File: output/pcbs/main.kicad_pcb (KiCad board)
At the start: 2 copper layers, 103.3 x 88.5 mm, 113 parts, among them SW1 CPG1316S01D02_reversible, SW10 CPG1316S01D02_reversible, SW11 CPG1316S01D02_reversible, SW12 CPG1316S01D02_reversible, SW13 CPG1316S01D02_reversible, SW14 CPG1316S01D02_reversible, SW15 CPG1316S01D02_reversible, SW16 CPG1316S01D02_reversible, SW17 CPG1316S01D02_reversible, SW18 CPG1316S01D02_reversible, SW2 CPG1316S01D02_reversible, SW3 CPG1316S01D02_reversible, SW4 CPG1316S01D02_reversible, SW5 CPG1316S01D02_reversible, SW6 CPG1316S01D02_reversible, SW7 CPG1316S01D02_reversible, SW8 CPG1316S01D02_reversible, SW9 CPG1316S01D02_reversible

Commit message: fix(routing): route pcb
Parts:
- removed the REF** at (2.80, 5.10)
- removed the REF** at (53.8, -6.80)
- removed the REF** at (53.8, -23.8)
- removed the REF** at (53.8, -40.8)
- removed the REF** at (70.8, -3.40)
- removed the REF** at (70.8, -20.4)
- removed the REF** at (70.8, -37.4)
- removed the REF** at (47.0, 13.6)
- removed the REF** at (64.5, 15.5)
- removed the REF** at (82.5, 19.9)
- removed the REF** at (-2.80, 5.10)
- removed the REF** at (2.80, -11.9)
- removed the REF** at (-2.80, -11.9)
- removed the REF** at (-2.80, -28.9)
- removed the REF** at (14.2, -8.50)
- removed the REF** at (14.2, -25.5)
- removed the REF** at (14.2, -42.5)
- removed the REF** at (31.2, -15.3)
- removed the REF** at (31.2, -32.3)
- removed the REF** at (31.2, -49.3)
- removed the REF** at (48.2, -6.80)
- removed the REF** at (48.2, -23.8)
- removed the REF** at (2.80, -28.9)
- removed the REF** at (48.2, -40.8)
- removed the REF** at (65.2, -3.40)
- removed the REF** at (65.2, -20.4)
- removed the REF** at (65.2, -37.4)
- removed the REF** at (41.4, 13.6)
- removed the REF** at (59.0, 14.5)
- removed the REF** at (77.7, 17.1)
- removed the REF** at (0.00, -3.67)
- removed the REF** at (0.00, -20.7)
- removed the REF** at (0.00, -37.7)
- removed the REF** at (19.8, -8.50)
- removed the REF** at (17.0, -17.3)
- removed the REF** at (17.0, -34.3)
- removed the REF** at (17.0, -51.3)
- removed the REF** at (34.0, -24.1)
- removed the REF** at (34.0, -41.1)
- removed the REF** at (34.0, -58.1)
- removed the REF** at (51.0, -15.6)
- removed the REF** at (51.0, -32.6)
- removed the REF** at (51.0, -49.6)
- removed the REF** at (68.0, -12.2)
- removed the REF** at (19.8, -25.5)
- removed the REF** at (68.0, -29.2)
- removed the REF** at (68.0, -46.2)
- removed the REF** at (44.2, 4.83)
- removed the REF** at (63.3, 6.37)
- removed the REF** at (84.5, 10.9)
- removed the REF** at (0.00, -2.67)
- removed the REF** at (0.00, -19.7)
- removed the REF** at (0.00, -36.7)
- removed the REF** at (17.0, -16.3)
- removed the REF** at (17.0, -33.3)
- removed the REF** at (19.8, -42.5)
- removed the REF** at (17.0, -50.3)
- removed the REF** at (34.0, -23.1)
- removed the REF** at (34.0, -40.1)
- removed the REF** at (34.0, -57.1)
- removed the REF** at (51.0, -14.6)
- removed the REF** at (51.0, -31.6)
- removed the REF** at (51.0, -48.6)
- removed the REF** at (68.0, -11.2)
- removed the REF** at (68.0, -28.2)
- removed the REF** at (68.0, -45.2)
- removed the REF** at (36.8, -15.3)
- removed the REF** at (44.2, 5.83)
- removed the REF** at (63.1, 7.35)
- removed the REF** at (84.0, 11.8)
- removed the REF** at (36.8, -32.3)
- removed the REF** at (36.8, -49.3)
- added REF**: VIA-0.6mm, VIA-0.6mm, F.Cu at (254.4, 153.2)
- added REF**: VIA-0.6mm, VIA-0.6mm, F.Cu at (220.4, 134.5)
- added REF**: VIA-0.6mm, VIA-0.6mm, F.Cu at (220.4, 151.5)
- added REF**: VIA-0.6mm, VIA-0.6mm, F.Cu at (234.7, 153.4)
- added REF**: VIA-0.6mm, VIA-0.6mm, F.Cu at (203.4, 166.1)
- added REF**: VIA-0.6mm, VIA-0.6mm, F.Cu at (257.2, 144.9)
- added REF**: VIA-0.6mm, VIA-0.6mm, F.Cu at (254.4, 154.2)
- added REF**: VIA-0.6mm, VIA-0.6mm, F.Cu at (220.4, 135.5)
- added REF**: VIA-0.6mm, VIA-0.6mm, F.Cu at (217.7, 143.2)
- added REF**: VIA-0.6mm, VIA-0.6mm, F.Cu at (206.2, 173.8)
- added REF**: VIA-0.6mm, VIA-0.6mm, F.Cu at (237.4, 162.7)
- added REF**: VIA-0.6mm, VIA-0.6mm, F.Cu at (223.2, 177.2)
- added REF**: VIA-0.6mm, VIA-0.6mm, F.Cu at (223.2, 143.2)
- added REF**: VIA-0.6mm, VIA-0.6mm, F.Cu at (274.2, 182.3)
- added REF**: VIA-0.6mm, VIA-0.6mm, F.Cu at (271.4, 139.6)
- added REF**: VIA-0.6mm, VIA-0.6mm, F.Cu at (200.7, 173.8)
- added REF**: VIA-0.6mm, VIA-0.6mm, F.Cu at (268.6, 165.3)
- added REF**: VIA-0.6mm, VIA-0.6mm, F.Cu at (254.4, 137.2)
- added REF**: VIA-0.6mm, VIA-0.6mm, F.Cu at (268.6, 148.3)
- added REF**: VIA-0.6mm, VIA-0.6mm, F.Cu at (271.4, 173.6)
- added REF**: VIA-0.6mm, VIA-0.6mm, F.Cu at (240.2, 136.4)
- added REF**: VIA-0.6mm, VIA-0.6mm, F.Cu at (257.2, 178.9)
- added REF**: VIA-0.6mm, VIA-0.6mm, F.Cu at (237.4, 161.7)
- added REF**: VIA-0.6mm, VIA-0.6mm, F.Cu at (220.4, 168.5)
- added REF**: VIA-0.6mm, VIA-0.6mm, F.Cu at (271.4, 140.6)
- added REF**: VIA-0.6mm, VIA-0.6mm, F.Cu at (286.0, 205.7)
- added REF**: VIA-0.6mm, VIA-0.6mm, F.Cu at (274.2, 165.3)
- added REF**: VIA-0.6mm, VIA-0.6mm, F.Cu at (217.7, 160.2)
- added REF**: VIA-0.6mm, VIA-0.6mm, F.Cu at (251.7, 144.9)
- added REF**: VIA-0.6mm, VIA-0.6mm, F.Cu at (200.7, 190.8)
- added REF**: VIA-0.6mm, VIA-0.6mm, F.Cu at (254.4, 136.2)
- added REF**: VIA-0.6mm, VIA-0.6mm, F.Cu at (237.4, 127.7)
- added REF**: VIA-0.6mm, VIA-0.6mm, F.Cu at (251.7, 178.9)
- added REF**: VIA-0.6mm, VIA-0.6mm, F.Cu at (234.7, 136.4)
- added REF**: VIA-0.6mm, VIA-0.6mm, F.Cu at (250.4, 199.3)
- added REF**: VIA-0.6mm, VIA-0.6mm, F.Cu at (247.7, 190.6)
- added REF**: VIA-0.6mm, VIA-0.6mm, F.Cu at (240.2, 170.4)
- added REF**: VIA-0.6mm, VIA-0.6mm, F.Cu at (266.6, 193.1)
- added REF**: VIA-0.6mm, VIA-0.6mm, F.Cu at (281.1, 202.9)
- added REF**: VIA-0.6mm, VIA-0.6mm, F.Cu at (203.4, 149.1)
- added REF**: VIA-0.6mm, VIA-0.6mm, F.Cu at (244.8, 199.3)
- added REF**: VIA-0.6mm, VIA-0.6mm, F.Cu at (234.7, 170.4)
- added REF**: VIA-0.6mm, VIA-0.6mm, F.Cu at (203.4, 148.1)
- added REF**: VIA-0.6mm, VIA-0.6mm, F.Cu at (271.4, 156.6)
- added REF**: VIA-0.6mm, VIA-0.6mm, F.Cu at (254.4, 170.2)
- added REF**: VIA-0.6mm, VIA-0.6mm, F.Cu at (274.2, 148.3)
- added REF**: VIA-0.6mm, VIA-0.6mm, F.Cu at (237.4, 144.7)
- added REF**: VIA-0.6mm, VIA-0.6mm, F.Cu at (287.9, 196.7)
- added REF**: VIA-0.6mm, VIA-0.6mm, F.Cu at (271.4, 174.6)
- added REF**: VIA-0.6mm, VIA-0.6mm, F.Cu at (203.4, 183.1)
- added REF**: VIA-0.6mm, VIA-0.6mm, F.Cu at (206.2, 156.8)
- added REF**: VIA-0.6mm, VIA-0.6mm, F.Cu at (203.4, 165.1)
- added REF**: VIA-0.6mm, VIA-0.6mm, F.Cu at (287.4, 197.6)
- added REF**: VIA-0.6mm, VIA-0.6mm, F.Cu at (251.7, 161.9)
- added REF**: VIA-0.6mm, VIA-0.6mm, F.Cu at (237.4, 128.7)
- added REF**: VIA-0.6mm, VIA-0.6mm, F.Cu at (203.4, 182.1)
- added REF**: VIA-0.6mm, VIA-0.6mm, F.Cu at (206.2, 190.8)
- added REF**: VIA-0.6mm, VIA-0.6mm, F.Cu at (237.4, 145.7)
- added REF**: VIA-0.6mm, VIA-0.6mm, F.Cu at (266.7, 192.1)
- added REF**: VIA-0.6mm, VIA-0.6mm, F.Cu at (217.7, 177.2)
- added REF**: VIA-0.6mm, VIA-0.6mm, F.Cu at (254.4, 171.2)
- added REF**: VIA-0.6mm, VIA-0.6mm, F.Cu at (220.4, 169.5)
- added REF**: VIA-0.6mm, VIA-0.6mm, F.Cu at (268.0, 201.2)
- added REF**: VIA-0.6mm, VIA-0.6mm, F.Cu at (200.7, 156.8)
- added REF**: VIA-0.6mm, VIA-0.6mm, F.Cu at (257.2, 161.9)
- added REF**: VIA-0.6mm, VIA-0.6mm, F.Cu at (247.7, 191.6)
- added REF**: VIA-0.6mm, VIA-0.6mm, F.Cu at (271.4, 157.6)
- added REF**: VIA-0.6mm, VIA-0.6mm, F.Cu at (268.6, 182.3)
- added REF**: VIA-0.6mm, VIA-0.6mm, F.Cu at (240.2, 153.4)
- added REF**: VIA-0.6mm, VIA-0.6mm, F.Cu at (220.4, 152.5)
- added REF**: VIA-0.6mm, VIA-0.6mm, F.Cu at (223.2, 160.2)
- added REF**: VIA-0.6mm, VIA-0.6mm, F.Cu at (262.5, 200.3)
- _73: moved to F.Cu
- moved SW17 275.5 mm to (266.1, 195.7)
- moved D18 275.5 mm to (283.6, 204.3)
- moved SW18 275.5 mm to (286.1, 199.9)
- moved D1 275.5 mm to (203.4, 190.8)
- moved D10 275.5 mm to (254.4, 178.9)
- moved D11 275.5 mm to (254.4, 161.9)
- moved D12 275.5 mm to (254.4, 144.9)
- moved D13 275.5 mm to (271.4, 182.3)
- moved D14 275.5 mm to (271.4, 165.3)
- moved D15 275.5 mm to (271.4, 148.3)
- moved D16 275.5 mm to (247.7, 199.3)
- moved D2 275.5 mm to (203.4, 173.8)
- moved D3 275.5 mm to (203.4, 156.8)
- moved D4 275.5 mm to (220.4, 177.2)
- moved D5 275.5 mm to (220.4, 160.2)
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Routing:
- net P4: track 0.00 -> 212.1 mm
- net P10: track 0.00 -> 166.3 mm
- net P9: track 0.00 -> 165.7 mm
- net P0: track 0.00 -> 155.8 mm
- net P1: track 0.00 -> 130.0 mm
- net P2: track 0.00 -> 113.3 mm
- net P8: track 0.00 -> 110.5 mm
- net P3: track 0.00 -> 63.8 mm
- net P5: track 0.00 -> 60.4 mm
- net ring_home: track 0.00 -> 54.3 mm
- net RAW: track 0.00 -> 26.9 mm
- net pinky_home: track 0.00 -> 17.5 mm
- net ring_bottom: track 0.00 -> 12.5 mm
- net inner_home: track 0.00 -> 12.5 mm
- net inner_top: track 0.00 -> 12.5 mm
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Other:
- board size 103.3 x 88.5 mm -> 103.3 x 89 mm
- net class Default removed

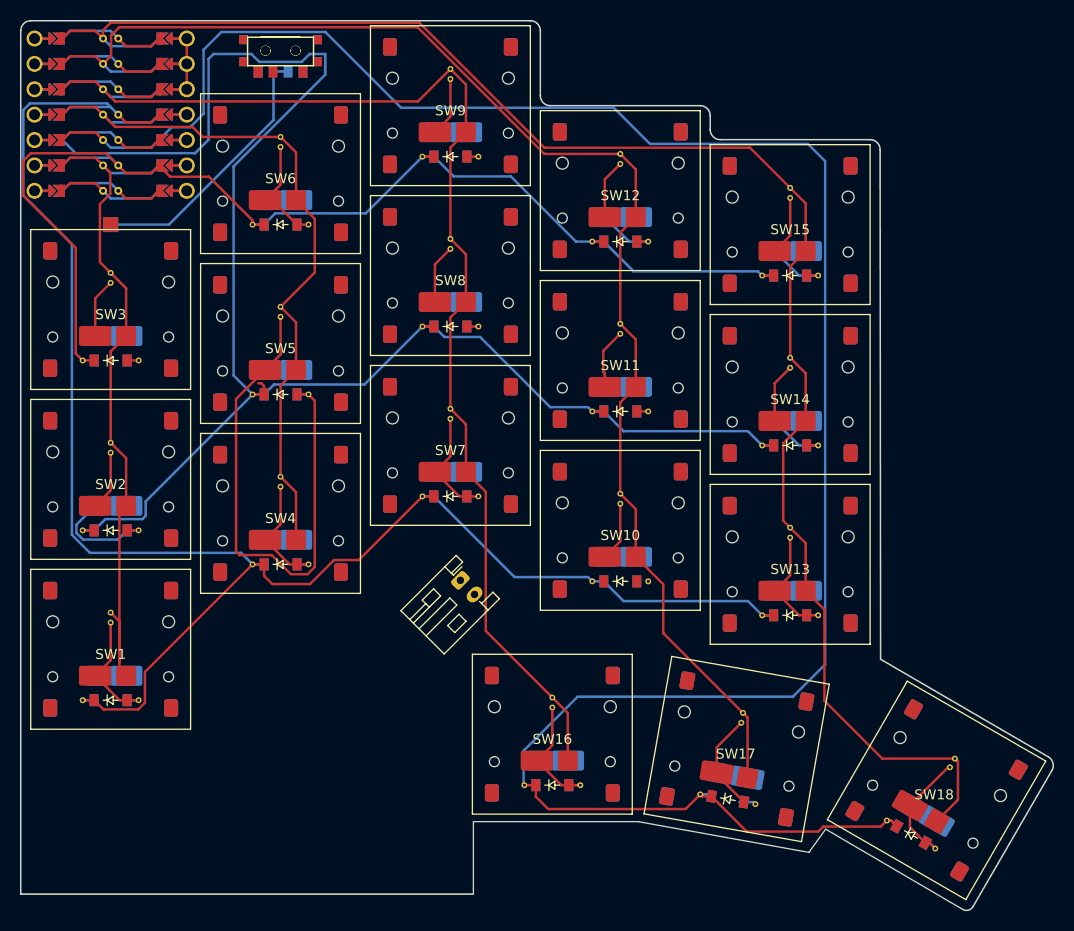
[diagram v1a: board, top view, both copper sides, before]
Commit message: feat(3dmodel): add 3d model of swtich
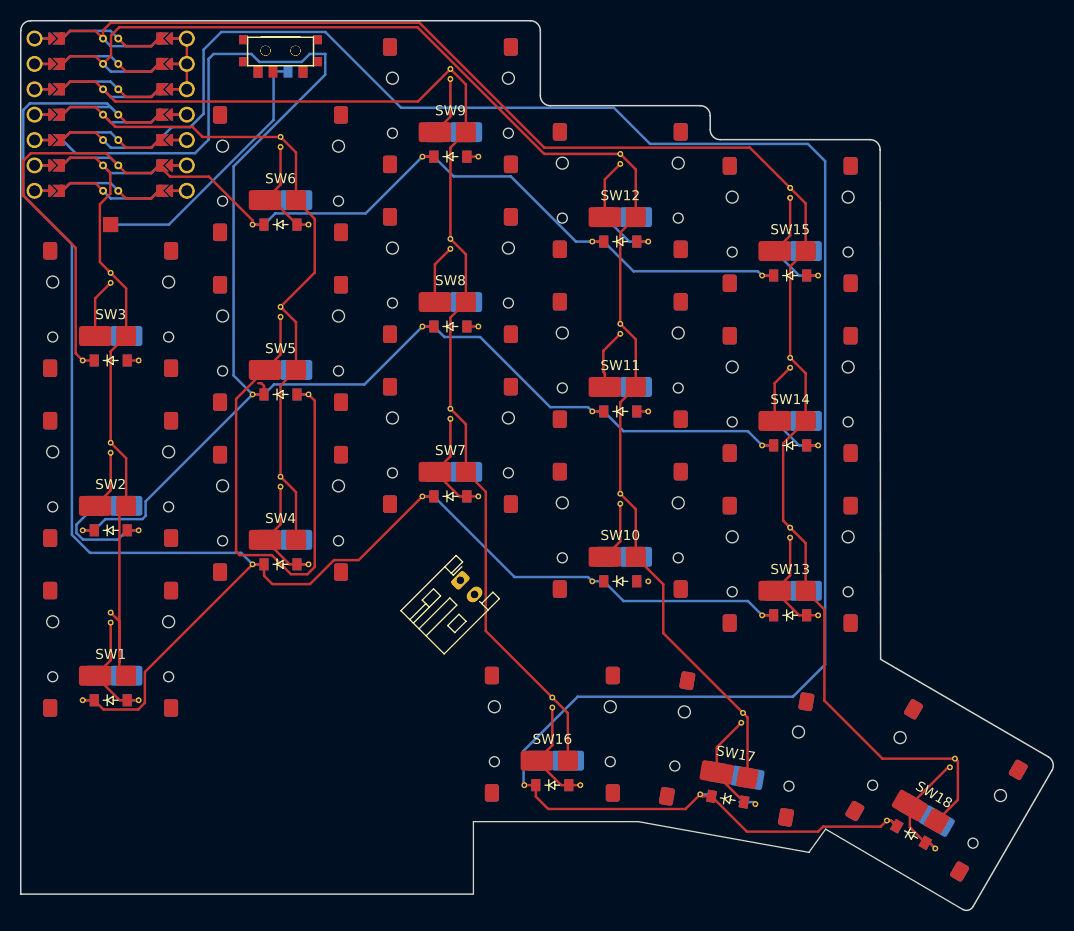
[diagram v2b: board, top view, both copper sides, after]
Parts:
- SW1, SW10, SW11, SW12, SW13, SW14, SW15, SW16, SW17, SW18, SW2, SW3, SW4, SW5, SW6, SW7, SW8, SW9: value CPG1316S01D02_reversible -> CPG1316S01D02_reversible_mikefives; footprint CPG1316S01D02_reversible -> leptiosis:CPG1316S01D02_reversible_mikefives

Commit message: feat(gerber): add gerber files
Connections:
- _73 pad 1: pos -> BAT+
- _73 pad 2: B- -> GND
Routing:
- net BAT+: track 0.00 -> 141.1 mm, vias 0 -> 1
- net GND: track 0.00 -> 99.0 mm
- net P9: track 165.7 -> 146.5 mm
- net P10: track 166.3 -> 168.8 mm
- net RAW: track 26.9 -> 29.2 mm
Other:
- board size 103.3 x 89 mm -> 104.3 x 89 mm

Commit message: chore(silkscreen): add markings
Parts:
- D1, D10, D11, D12, D13, D14, D15, D16, D17, D18, D2, D3, D4, D5, D6, D7, D8, D9: footprint ComboDiode -> PCM_Diode_SMD_Handsoldering_AKL:D_SOD-123
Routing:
- net middle_top: track 7.11 -> 11.3 mm
- net middle_home: track 7.11 -> 11.3 mm
- net P2: track 113.3 -> 116.6 mm
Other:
- outline, holes or cut-outs redrawn
